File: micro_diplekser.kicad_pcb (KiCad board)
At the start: 2 copper layers, 21 x 15 mm, 13 parts, among them J1 Antenna [146 MHz|443MHz], J2 146 MHz, J3 443 MHz

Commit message: Last modifications
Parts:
- J2: renamed from J3; value 443 MHz -> 146 MHz
- J3: renamed from J2; value 146 MHz -> 443 MHz
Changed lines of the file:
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@@
 		(layer "F.Cu")
 		(at 71.2216 96.8864 90)
-		(property "Reference" "J2"
+		(property "Reference" "J3"
 			(at 0 -3.75 90)
 			(unlocked yes)
@@
 			)
 		)
-		(property "Value" "146 MHz"
+		(property "Value" "443 MHz"
 			(at 0 1 90)
 			(unlocked yes)
@@
 			(size 2.25 2)
 			(layers "F.Cu" "F.Paste" "F.Mask")
-			(net 7 "Net-(J2-In)")
+			(net 8 "Net-(J3-In)")
 			(pinfunction "In")
 			(pintype "passive")
@@
 			(layers "F.Cu" "F.Paste" "F.Mask")
 			(roundrect_rratio 0.25)
-			(net 8 "Net-(J3-In)")
+			(net 7 "Net-(J2-In)")
 			(pinfunction "2")
 			(pintype "passive")
@@
 		(layer "F.Cu")
 		(at 71.1976 89.114 90)
-		(property "Reference" "J3"
+		(property "Reference" "J2"
 			(at 0 -3.75 90)
 			(unlocked yes)
@@
 			)
 		)
-		(property "Value" "443 MHz"
+		(property "Value" "146 MHz"
 			(at 0 1 90)
 			(unlocked yes)
@@
 			(size 2.25 2)
 			(layers "F.Cu" "F.Paste" "F.Mask")
-			(net 8 "Net-(J3-In)")
+			(net 7 "Net-(J2-In)")
 			(pinfunction "In")
 			(pintype "passive")
@@
 			(layers "F.Cu" "F.Paste" "F.Mask")
 			(roundrect_rratio 0.25)
-			(net 7 "Net-(J2-In)")
+			(net 8 "Net-(J3-In)")
 			(pintype "passive")
 		)
@@
 	)
 	(segment
+		(start 70.1708 89.114)
+		(end 68.12235 89.114)
+		(width 2.25)
+		(layer "F.Cu")
+		(net 7)
+	)
+	(segment
 		(start 67.57235 96.92885)
 		(end 67.564 96.9372)
 		(width 2.25)
 		(layer "F.Cu")
-		(net 7)
+		(net 8)
 	)
 	(segment
@@
 		(width 2.25)
 		(layer "F.Cu")
-		(net 7)
+		(net 8)
 	)
 	(segment
@@
 		(width 2.25)
 		(layer "F.Cu")
-		(net 7)
-	)
-	(segment
-		(start 70.1708 89.114)
-		(end 68.12235 89.114)
-		(width 2.25)
-		(layer "F.Cu")

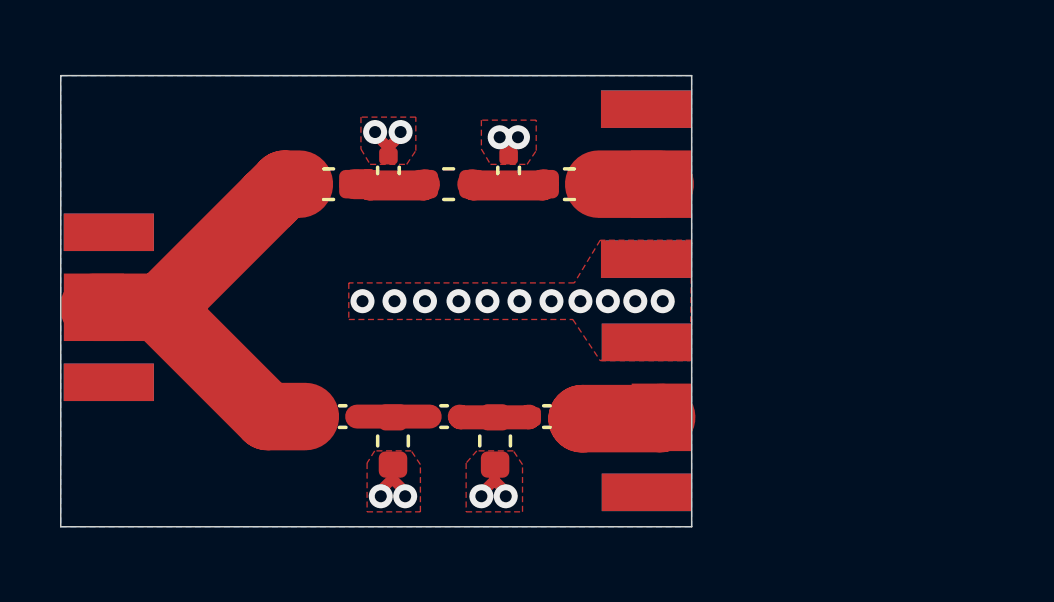
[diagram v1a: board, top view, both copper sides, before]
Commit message: Improved version - better S1.1 S2.2 and S3.3 parameters, bigger width and dBm, but decrease isolation between port 3 and port 2 by 5 dBm. Made whole design with 0603 components, not mixing size like in previous design
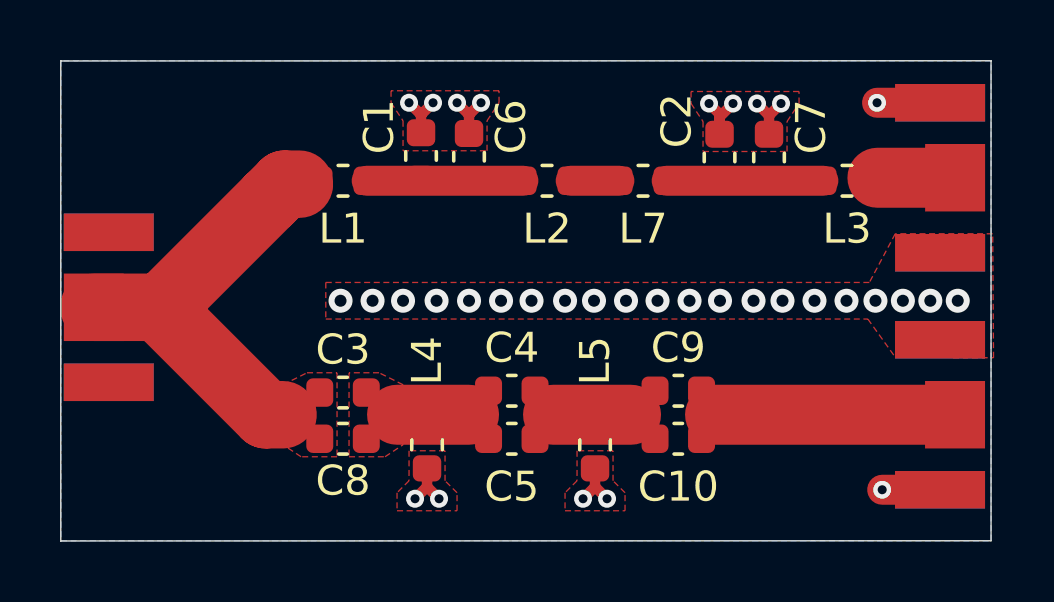
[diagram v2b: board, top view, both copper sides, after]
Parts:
- added C10: 0.8 pF, Capacitor_SMD:C_0603_1608Metric, F.Cu at (70.8, 97.6)
- added C6: 2.7 pF, Capacitor_SMD:C_0603_1608Metric, F.Cu at (63.8, 88.2)
- added C7: 2.7 pF, Capacitor_SMD:C_0603_1608Metric, F.Cu at (73.8, 88.2)
- added C8: 0.5 pF, Capacitor_SMD:C_0603_1608Metric, F.Cu at (59.6, 97.6)
- added C9: 6.8 pF, Capacitor_SMD:C_0603_1608Metric, F.Cu at (70.8, 96.0)
- added L7: 7.5 nH, Inductor_SMD:L_0603_1608Metric, F.Cu at (69.6, 89.0)
- C1, C2: value 18 pF -> 20 pF; footprint Capacitor_SMD:C_0402_1005Metric -> Capacitor_SMD:C_0603_1608Metric
- C3: value 4.7 pF -> 3.9pF; footprint Capacitor_SMD:C_0402_1005Metric -> Capacitor_SMD:C_0603_1608Metric
- C4: value 3.3 pF -> 2.7 pF; footprint Capacitor_SMD:C_0402_1005Metric -> Capacitor_SMD:C_0603_1608Metric
- C5: value 5.6 pF -> 0.5 pF; footprint Capacitor_SMD:C_0402_1005Metric -> Capacitor_SMD:C_0603_1608Metric
- L1, L3: value 68 nH -> 51 nH
- L2: value 120 nH -> 82 nH
- L4, L5: value 15 nH -> 18 nH
- moved J2 9.81 mm to (81.0, 88.9)
- moved J3 9.78 mm to (81.0, 96.8)
- moved L3 9.25 mm to (76.4, 89.0)
- moved C2 7.04 mm to (72.2, 88.2)
- moved L5 3.33 mm to (68.0, 97.8)
- moved L2 3.28 mm to (66.4, 89.0)
- moved C4 2.41 mm to (65.2, 96.0)
- moved C5 1.39 mm to (65.2, 97.6)
- moved C1 1.19 mm to (62.2, 88.2)
- moved L4 1.14 mm to (62.4, 97.8)
- moved C3 0.80 mm to (59.6, 96.1)
- moved L1 0.49 mm to (59.6, 89.0)
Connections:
- C4 pad 2: Net-(C4-Pad2) -> Net-(C10-Pad1)
- C5 pad 1: Net-(C4-Pad2) -> Net-(C3-Pad2)
- C5 pad 2: Net-(J3-In) -> Net-(C10-Pad1)
- L2 pad 2: Net-(C2-Pad1) -> Net-(L2-Pad2)
- L5 pad 2: Net-(C4-Pad2) -> Net-(C10-Pad1)
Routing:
- net GND: track 6.33 -> 15.7 mm, vias 19 -> 35
- net Net-(J3-In): track 2.68 -> 7.91 mm
- net Net-(C1-Pad1): track 2.40 -> 5.22 mm
- net Net-(C2-Pad1): track 2.48 -> 5.22 mm
- net Net-(C10-Pad1): track 0.00 -> 2.60 mm
- net Net-(C4-Pad2): track 2.41 -> 0.00 mm
- net Net-(L2-Pad2): track 0.00 -> 1.62 mm
- net Net-(J1-In): track 15.0 -> 14.2 mm
- net Net-(J2-In): track 2.05 -> 2.59 mm
- added copper zone on F.Cu, net Net-(C3-Pad2)
- added copper zone on F.Cu, net Net-(J1-In)
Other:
- board size 21 x 15 mm -> 31 x 16 mm
- board text added: "146 MHz"
- board text added: "434 MHz"
- board text added: "Antenna"

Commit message: v2
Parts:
- moved J3 0.17 mm to (81.2, 96.7)
- moved J2 0.13 mm to (81.1, 88.9)
